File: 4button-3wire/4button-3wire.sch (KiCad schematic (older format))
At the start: 19 parts, among them J1 AudioJack3_Ground, J2 AudioJack3_Ground, SW1 SW_Push, SW2 SW_Push, SW3 SW_Push, SW4 SW_Push

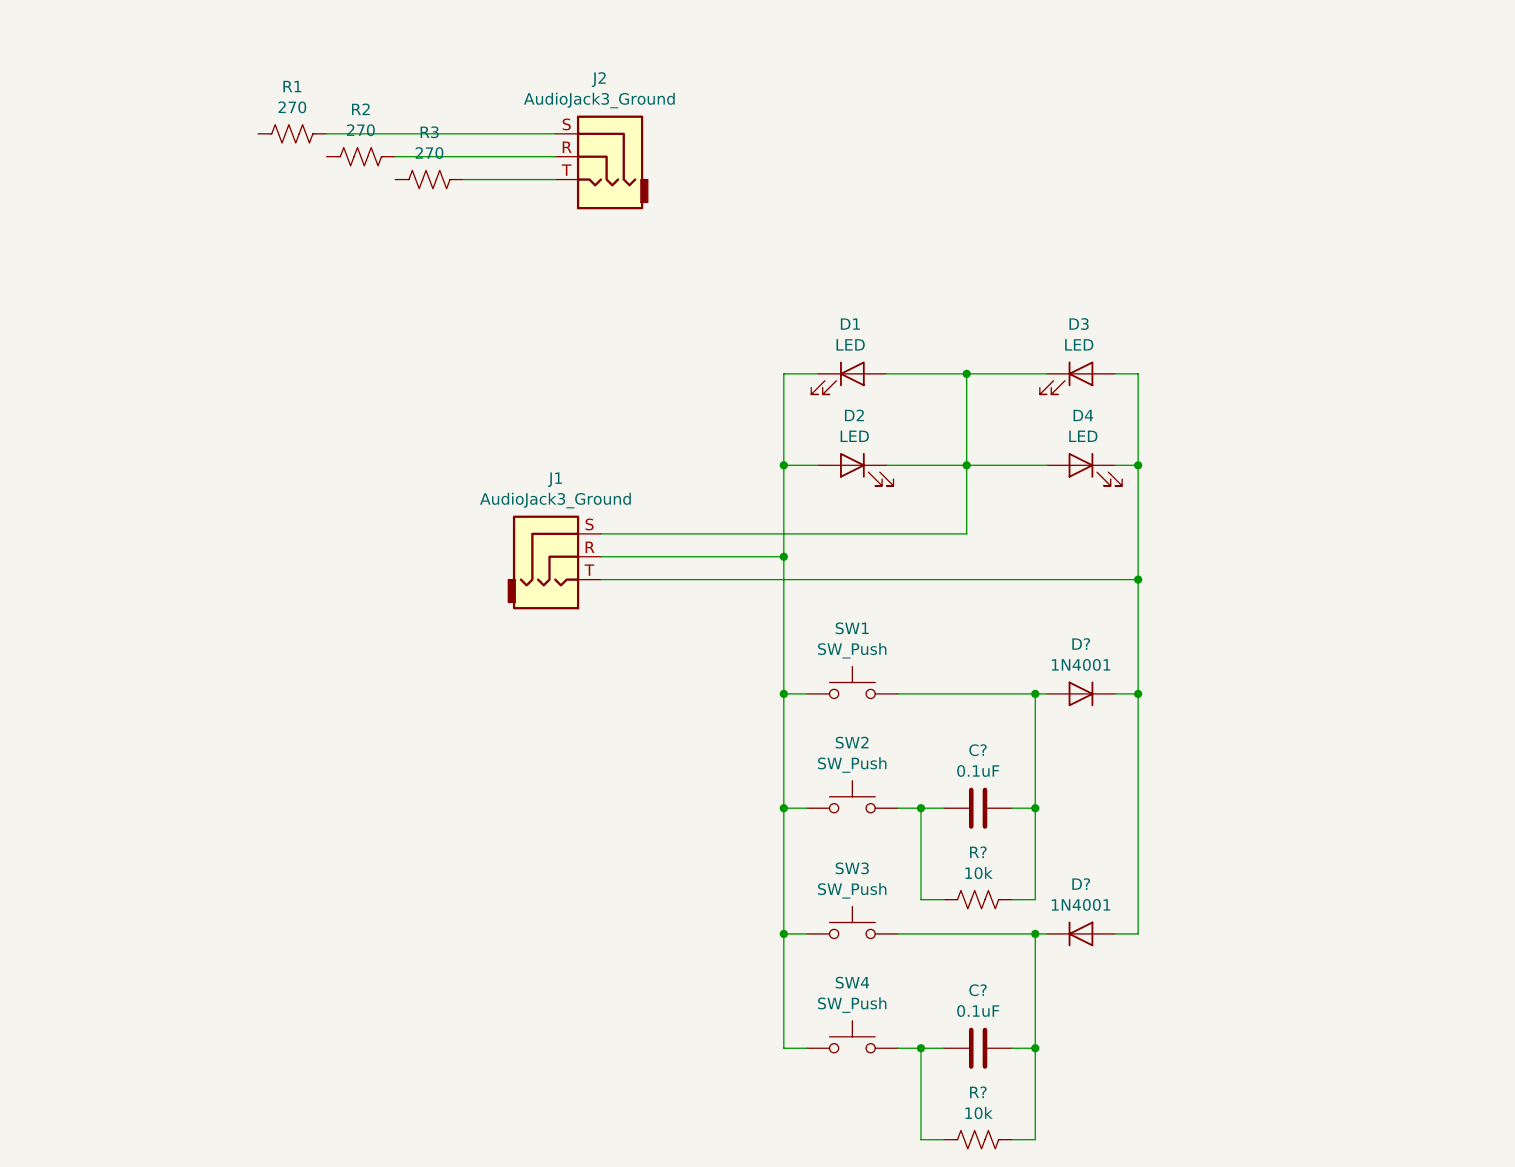
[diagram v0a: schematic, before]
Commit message: Share the RC circuit between both button pairs
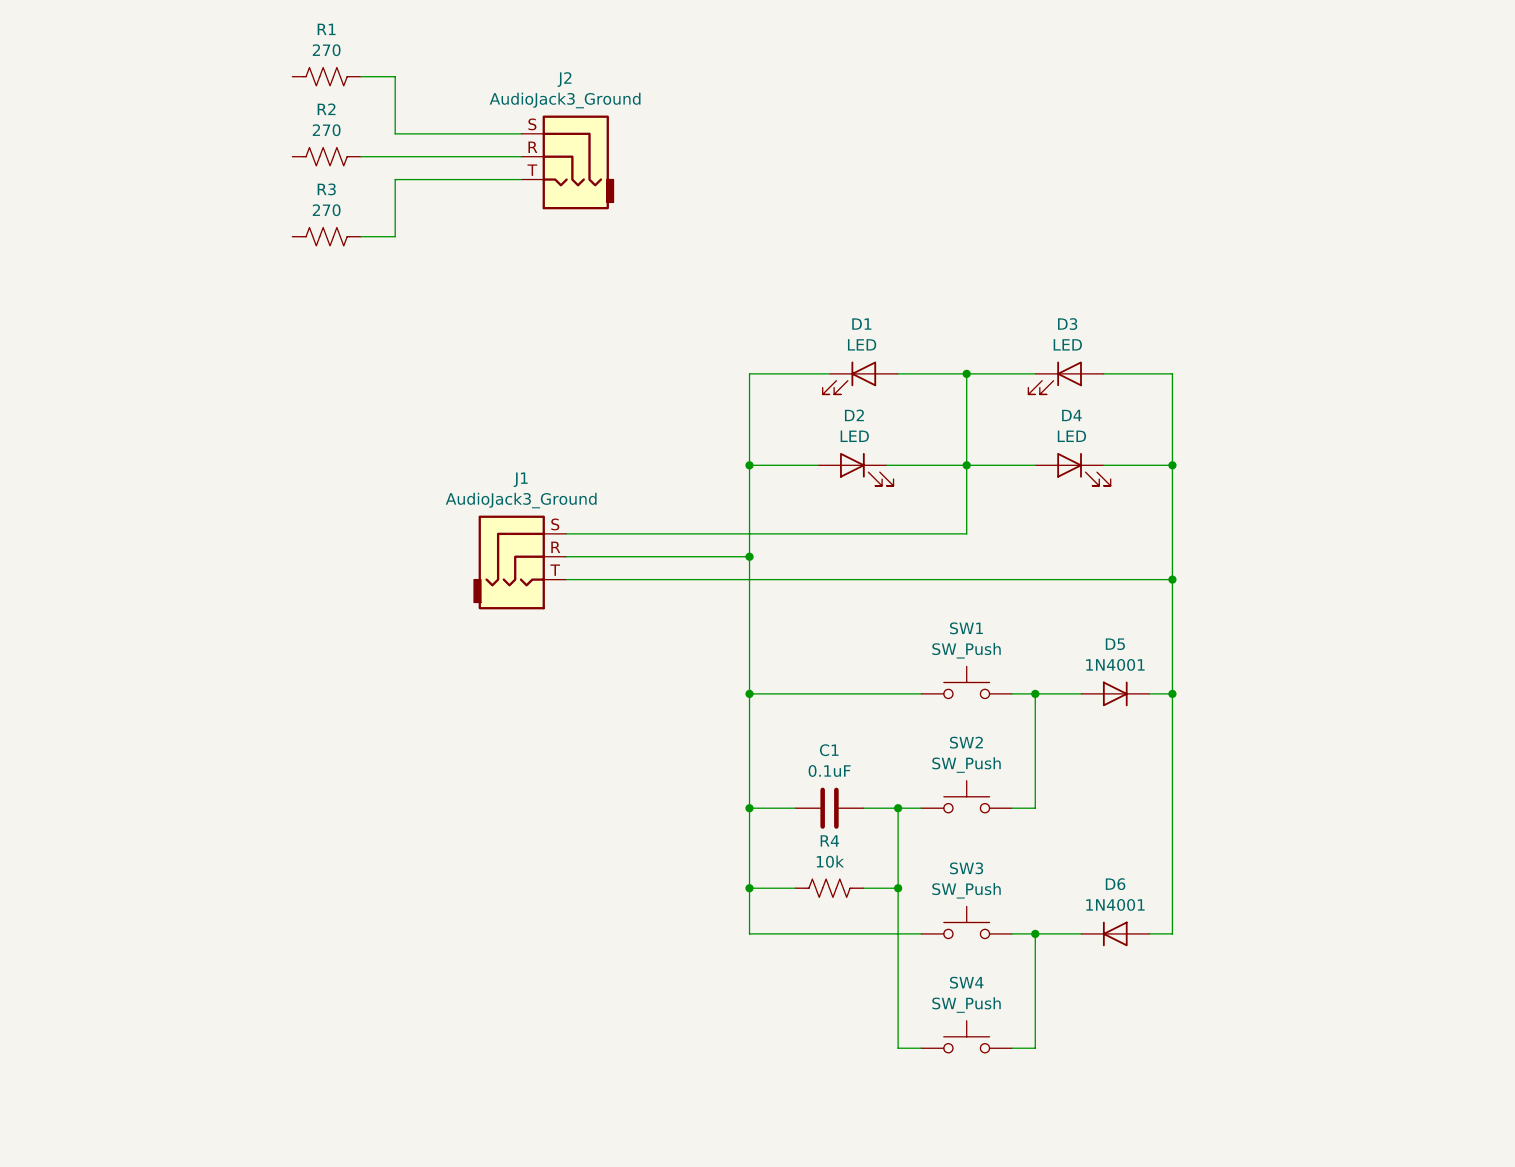
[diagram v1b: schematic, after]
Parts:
- removed C?: 0.1uF, symbol Device:C
- removed R?: 10k, symbol Device:R_US
- gave numbers to parts that had none: 4
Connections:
- net at D1.1 (K), D2.2 (A), J1.R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: now also C1.2, R4.2; no longer SW2.1, SW4.1
- net at D5.2 (A), SW1.2: now also SW2.2; no longer C1.1, R4.1
- net at D6.1 (K), SW3.2: now also SW4.2
- new net: C1.1, R4.1, SW2.1, SW4.1
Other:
- moved on the sheet: C1, D1, D3, D4, D5, D6, J1, J2, R1, R2, R3, R4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

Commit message: Mostly routed
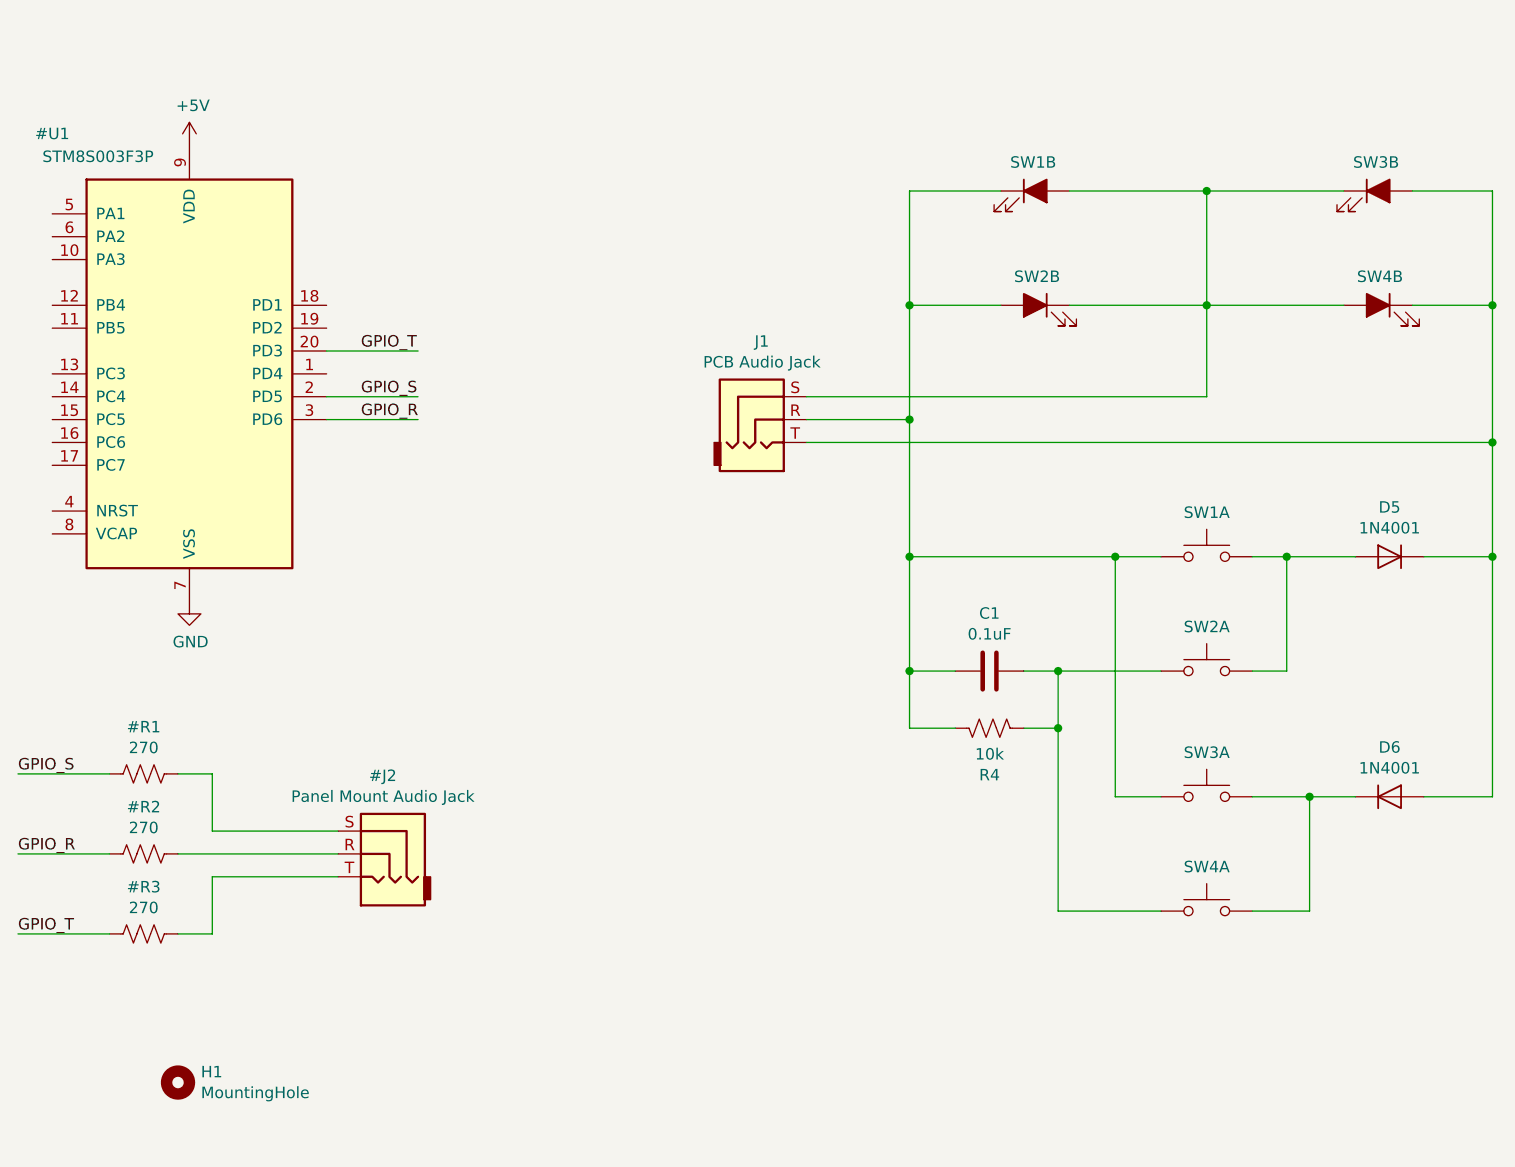
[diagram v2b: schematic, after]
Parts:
- removed D1, D2, D3, D4: LED, symbol Device:LED
- removed J2: AudioJack3_Ground, symbol Connector:AudioJack3_Ground
- removed R1, R2, R3: 270, symbol Device:R_US
- removed SW1, SW2, SW3, SW4: SW_Push, symbol Switch:SW_Push
- added H1: MountingHole, MountingHole:MountingHole_3.2mm_M3, symbol Mechanical:MountingHole
- added SW1, SW2, SW3, SW4: SW_Push_LED_Separate, SW_LightedPush_ITW_Series39, symbol 4button-3wire:SW_Push_LED_Separate
- C1: footprint (none) -> Capacitor_THT:C_Disc_D4.7mm_W2.5mm_P5.00mm
- J1: value AudioJack3_Ground -> PCB Audio Jack; footprint (none) -> 4button-3wire:Jack_3.5mm_7mmSpacing
- R4: footprint (none) -> Resistor_THT:R_Axial_DIN0207_L6.3mm_D2.5mm_P10.16mm_Horizontal
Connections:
- net labels added: +5V, 270, GND, GPIO_R, GPIO_S, GPIO_T, Panel Mount Audio Jack, STM8S003F3P
- wire segments 50 -> 57
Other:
- moved on the sheet: C1, D5, D6, J1, R4

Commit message: Changed Switch Footprint
Made a new footprint with smaller size pads
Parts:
- SW1, SW2, SW3, SW4: footprint SW_LightedPush_ITW_Series39 -> 4button-3wire:SW_LightedPush_ITW_Series39_SmallPads
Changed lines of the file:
@@
 F 0 "SW1" H 7650 3893 50  0000 C CNN
 F 1 "SW_Push_LED_Separate" H 7650 3550 50  0001 C CNN
-F 2 "SW_LightedPush_ITW_Series39" H 7550 3600 50  0001 C CNN
+F 2 "4button-3wire:SW_LightedPush_ITW_Series39_SmallPads" H 7550 3600 50  0001 C CNN
 F 3 "" H 7550 3600 50  0001 C CNN
 	1    7650 3700
@@
 F 0 "SW1" H 6891 2225 50  0000 C CNN
 F 1 "SW_Push_LED_Separate" H 6900 1950 50  0001 C CNN
-F 2 "SW_LightedPush_ITW_Series39" H 6800 2000 50  0001 C CNN
+F 2 "4button-3wire:SW_LightedPush_ITW_Series39_SmallPads" H 6800 2000 50  0001 C CNN
 F 3 "" H 6800 2000 50  0001 C CNN
 	2    6900 2100
@@
 F 0 "SW2" H 7650 4393 50  0000 C CNN
 F 1 "SW_Push_LED_Separate" H 7650 4050 50  0001 C CNN
-F 2 "SW_LightedPush_ITW_Series39" H 7550 4100 50  0001 C CNN
+F 2 "4button-3wire:SW_LightedPush_ITW_Series39_SmallPads" H 7550 4100 50  0001 C CNN
 F 3 "" H 7550 4100 50  0001 C CNN
 	1    7650 4200
@@
 F 0 "SW2" H 6892 2725 50  0000 C CNN
 F 1 "SW_Push_LED_Separate" H 6900 2450 50  0001 C CNN
-F 2 "SW_LightedPush_ITW_Series39" H 6800 2500 50  0001 C CNN
+F 2 "4button-3wire:SW_LightedPush_ITW_Series39_SmallPads" H 6800 2500 50  0001 C CNN
 F 3 "" H 6800 2500 50  0001 C CNN
 	2    6900 2600
@@
 F 0 "SW3" H 7650 4943 50  0000 C CNN
 F 1 "SW_Push_LED_Separate" H 7650 4600 50  0001 C CNN
-F 2 "SW_LightedPush_ITW_Series39" H 7550 4650 50  0001 C CNN
+F 2 "4button-3wire:SW_LightedPush_ITW_Series39_SmallPads" H 7550 4650 50  0001 C CNN
 F 3 "" H 7550 4650 50  0001 C CNN
 	1    7650 4750
@@
 F 0 "SW3" H 8391 2225 50  0000 C CNN
 F 1 "SW_Push_LED_Separate" H 8400 1950 50  0001 C CNN
-F 2 "SW_LightedPush_ITW_Series39" H 8300 2000 50  0001 C CNN
+F 2 "4button-3wire:SW_LightedPush_ITW_Series39_SmallPads" H 8300 2000 50  0001 C CNN
 F 3 "" H 8300 2000 50  0001 C CNN
 	2    8400 2100
@@
 F 0 "SW4" H 7650 5443 50  0000 C CNN
 F 1 "SW_Push_LED_Separate" H 7650 5100 50  0001 C CNN
-F 2 "SW_LightedPush_ITW_Series39" H 7550 5150 50  0001 C CNN
+F 2 "4button-3wire:SW_LightedPush_ITW_Series39_SmallPads" H 7550 5150 50  0001 C CNN
 F 3 "" H 7550 5150 50  0001 C CNN
 	1    7650 5250
@@
 F 0 "SW4" H 8392 2725 50  0000 C CNN
 F 1 "SW_Push_LED_Separate" H 8400 2450 50  0001 C CNN
-F 2 "SW_LightedPush_ITW_Series39" H 8300 2500 50  0001 C CNN
+F 2 "4button-3wire:SW_LightedPush_ITW_Series39_SmallPads" H 8300 2500 50  0001 C CNN
 F 3 "" H 8300 2500 50  0001 C CNN
 	2    8400 2600
